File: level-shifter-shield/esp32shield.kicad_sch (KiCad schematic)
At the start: 18 parts, among them J1 Power_Terminal, J2 Screw_Terminal_01x02, J3 Screw_Terminal_01x02, J4 Screw_Terminal_01x02, J5 Screw_Terminal_01x02, J6 Conn_01x19_Female, J7 Conn_01x19_Female, J8 Conn_02x19_Counter_Clockwise, U2 74HC245

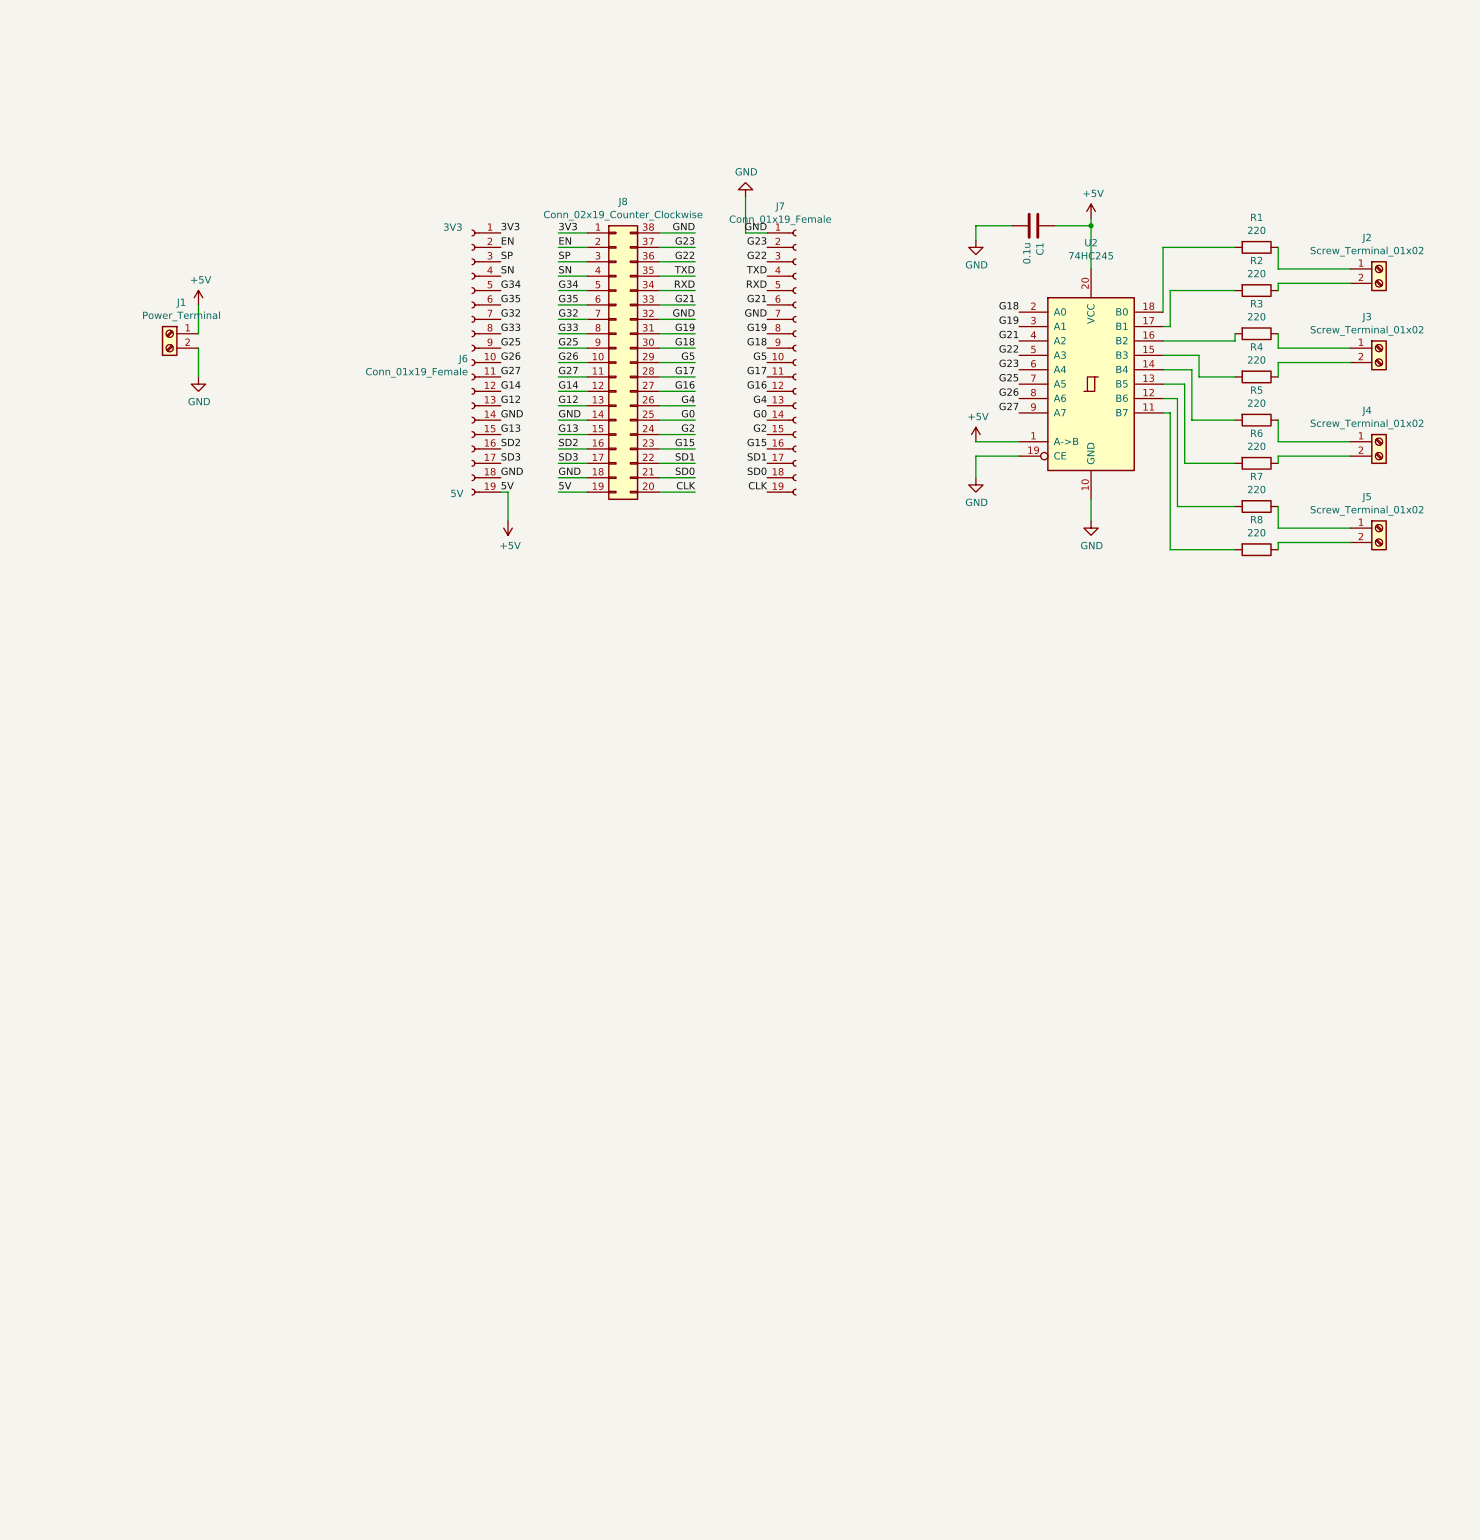
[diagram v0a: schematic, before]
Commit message: Finish new level shifter shield schematic
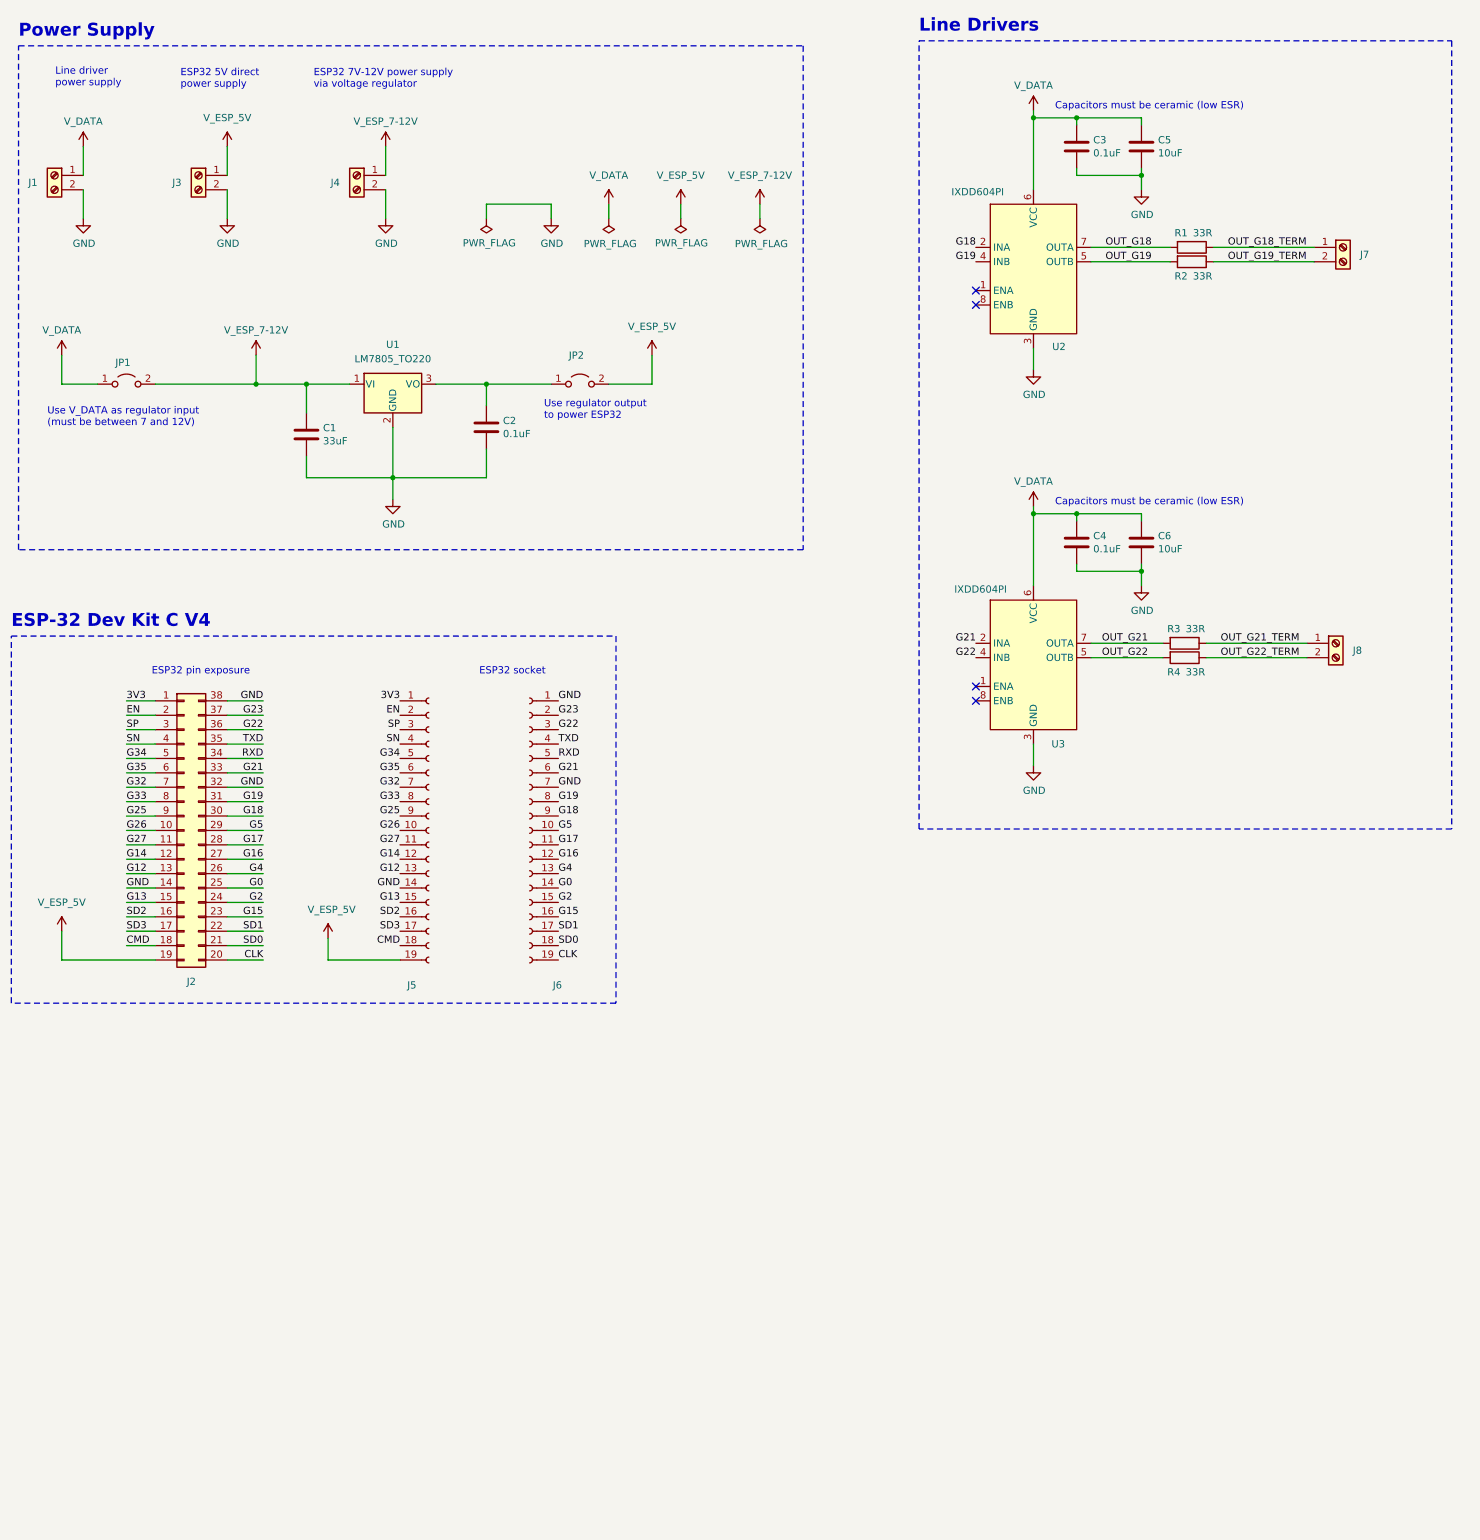
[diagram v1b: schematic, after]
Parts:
- removed J5: Screw_Terminal_01x02, TerminalBlock_Phoenix:TerminalBlock_Phoenix_MKDS-1,5-2-5.08_1x02_P5.08mm_Horizontal, symbol Connector:Screw_Terminal_01x02
- removed J6, J7: Conn_01x19_Female, Connector_PinSocket_2.54mm:PinSocket_1x19_P2.54mm_Vertical, symbol esp32shield-rescue:Conn_01x19_Female-Connector
- removed R5, R6, R7, R8: 220, Resistor_THT:R_Axial_DIN0207_L6.3mm_D2.5mm_P2.54mm_Vertical, symbol Device:R
- removed U2: 74HC245, Package_DIP:DIP-20_W7.62mm, symbol 74xx:74HC245
- added C2, C3, C4: 0.1uF, Capacitor_THT:C_Disc_D3.0mm_W1.6mm_P2.50mm, symbol Device:C
- added C5, C6: 10uF, Capacitor_THT:C_Disc_D3.0mm_W1.6mm_P2.50mm, symbol Device:C
- added J1: Power_Terminal, TerminalBlock_Phoenix:TerminalBlock_Phoenix_MKDS-1,5-2_1x02_P5.00mm_Horizontal, symbol Connector:Screw_Terminal_01x02
- added J5, J6: Conn_01x19_Socket, symbol Connector:Conn_01x19_Socket
- added JP1, JP2: Jumper_2_Open, symbol Jumper:Jumper_2_Open
- added U1: LM7805_TO220, Package_TO_SOT_THT:TO-220-3_Vertical, symbol Regulator_Linear:LM7805_TO220
- added U2, U3: IXDD604PI, Package_DIP:DIP-8_W7.62mm_Socket, symbol lib:IXDD604PI
- C1: value 0.1u -> 33uF
- J4: value Screw_Terminal_01x02 -> Power_Terminal; footprint TerminalBlock_Phoenix:TerminalBlock_Phoenix_MKDS-1,5-2-5.08_1x02_P5.08mm_Horizontal -> TerminalBlock_Phoenix:TerminalBlock_Phoenix_MKDS-1,5-2_1x02_P5.00mm_Horizontal
- R1, R2, R3, R4: value 220 -> 33R
- renumbered J8 to J2, J1 to J3, J2 to J7, J3 to J8
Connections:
- net 3V3: now also J5.1 (Pin_1)
- net CLK: now also J6.19 (Pin_19)
- net EN: now also J5.2 (Pin_2)
- net G0: now also J6.14 (Pin_14)
- net G12: now also J5.13 (Pin_13)
- net G13: now also J5.15 (Pin_15)
- net G14: now also J5.12 (Pin_12)
- net G15: now also J6.16 (Pin_16)
- net G16: now also J6.12 (Pin_12)
- net G17: now also J6.11 (Pin_11)
- net G18: now also J6.9 (Pin_9), U2.2 (INA)
- net G19: now also J6.8 (Pin_8), U2.4 (INB)
- net G2: now also J6.15 (Pin_15)
- net G21: now also J6.6 (Pin_6), U3.2 (INA)
- net G22: now also J6.3 (Pin_3), U3.4 (INB)
- net G23: now also J6.2 (Pin_2)
- net G25: now also J5.9 (Pin_9)
- net G26: now also J5.10 (Pin_10)
- net G27: now also J5.11 (Pin_11)
- net G32: now also J5.7 (Pin_7)
- net G33: now also J5.8 (Pin_8)
- net G34: now also J5.5 (Pin_5)
- net G35: now also J5.6 (Pin_6)
- net G4: now also J6.13 (Pin_13)
- net G5: now also J6.10 (Pin_10)
- net GND: now also J4.2 (Pin_2), C2.2, C3.2, C4.2, C5.2, C6.2, J1.2 (Pin_2), J5.14 (Pin_14), J6.1 (Pin_1), J6.7 (Pin_7), U1.2 (GND), U2.3 (GND), U3.3 (GND); no longer J2.18 (Pin_18)
- net RXD: now also J6.5 (Pin_5)
- net SD0: now also J6.18 (Pin_18)
- net SD1: now also J6.17 (Pin_17)
- net SD2: now also J5.16 (Pin_16)
- net SD3: now also J5.17 (Pin_17)
- net SN: now also J5.4 (Pin_4)
- net SP: now also J5.3 (Pin_3)
- net TXD: now also J6.4 (Pin_4)
- net OUT_G22: now reaches R4.2
- net OUT_G22: now also U3.5 (OUTB)
- net OUT_G21: now reaches R3.2
- net OUT_G21: now also U3.7 (OUTA)
- net OUT_G19: now reaches R2.2
- net OUT_G19: now also U2.5 (OUTB)
- net OUT_G18: now reaches R1.2
- net OUT_G18: now also U2.7 (OUTA)
- net OUT_G18_TERM: now reaches J7.1 (Pin_1), R1.1
- net OUT_G19_TERM: now reaches J7.2 (Pin_2), R2.1
- net OUT_G21_TERM: now reaches J8.1 (Pin_1), R3.1
- net OUT_G22_TERM: now reaches J8.2 (Pin_2), R4.1
- net V_ESP_7-12V: now reaches J4.1 (Pin_1)
- net V_ESP_7-12V: now also C1.1, JP1.2 (B), U1.1 (VI)
- net +5V renamed V_ESP_5V
- net V_ESP_5V: now also J5.19 (Pin_19), JP2.2 (B); no longer C1.1
- new net: C2.1, JP2.1 (A), U1.3 (VO)
- new net CMD: J2.18 (Pin_18), J5.18 (Pin_18)
- new net V_DATA: C3.1, C4.1, C5.1, C6.1, J1.1 (Pin_1), JP1.1 (A), U2.6 (VCC), U3.6 (VCC)
- no-connect marks 0 -> 4
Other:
- note added: "Capacitors must be ceramic (low ESR)"
- note added: "ESP-32 Dev Kit C V4"
- note added: "ESP32 5V direct power supply"
- note added: "ESP32 7V-12V power supply via voltage regulator"
- note added: "ESP32 pin exposure"
- note added: "ESP32 socket"
- note added: "Line Drivers"
- note added: "Line driver power supply"
- note added: "Power Supply"
- note added: "Use V_DATA as regulator input (must be between 7 and 12V)"
- note added: "Use regulator output to power ESP32"
- note removed: "3V3"
- note removed: "5V"
- moved on the sheet: J2, J3, J7, J8

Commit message: Finish level shifter shield layout without traces
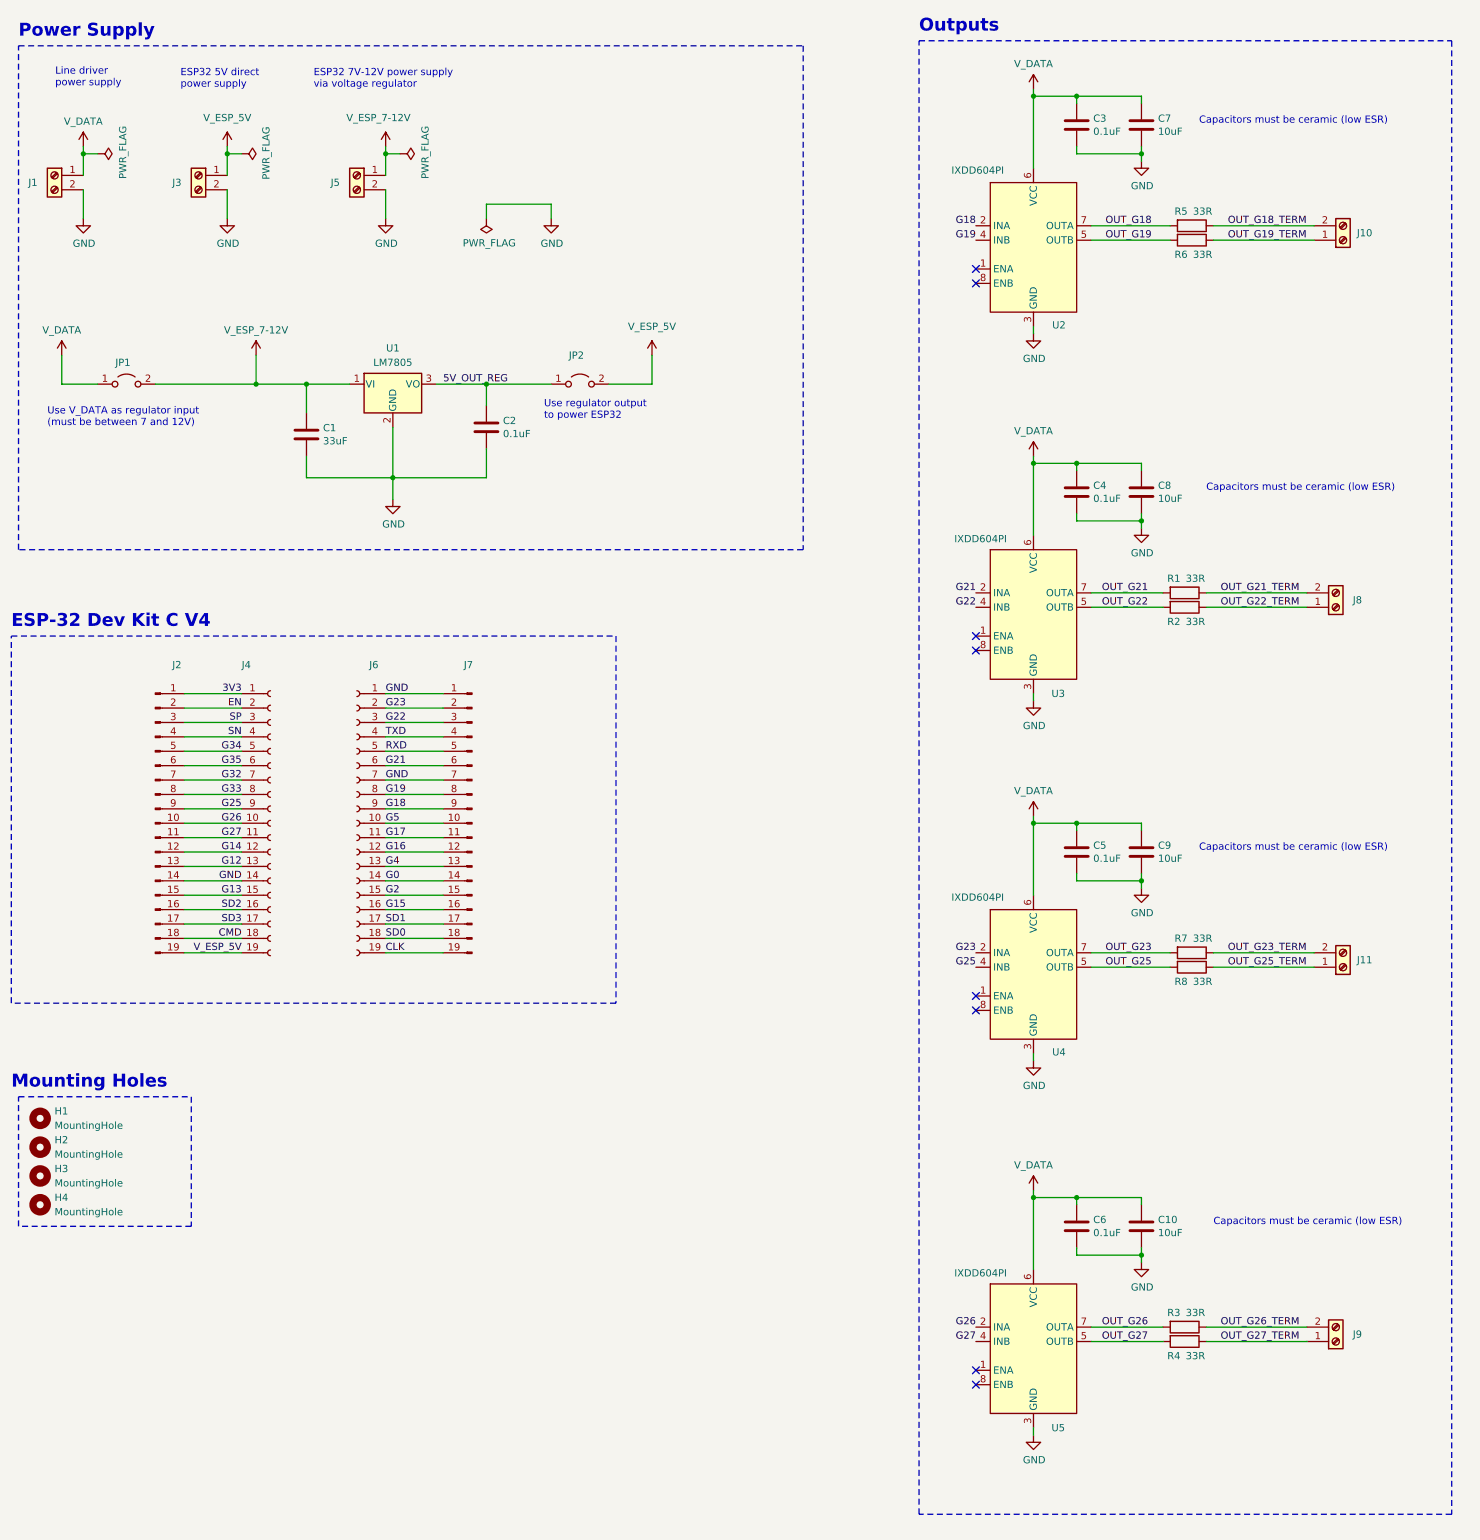
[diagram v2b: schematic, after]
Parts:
- removed J2: Conn_02x19_Counter_Clockwise, Connector_PinHeader_2.54mm:PinHeader_2x19_P2.54mm_Vertical, symbol Connector_Generic:Conn_02x19_Counter_Clockwise
- added C10, C9: 10uF, Capacitor_THT:C_Disc_D3.0mm_W1.6mm_P2.50mm, symbol Device:C
- added C5, C6: 0.1uF, Capacitor_THT:C_Disc_D3.0mm_W1.6mm_P2.50mm, symbol Device:C
- added H1, H2, H3, H4: MountingHole, MountingHole:MountingHole_2.2mm_M2, symbol Mechanical:MountingHole
- added J11, J9: Screw_Terminal_01x02, TerminalBlock_Phoenix:TerminalBlock_Phoenix_MKDS-1,5-2-5.08_1x02_P5.08mm_Horizontal, symbol Connector:Screw_Terminal_01x02
- added J2, J7: Conn_01x19_Pin, Connector_PinHeader_2.54mm:PinHeader_1x19_P2.54mm_Vertical, symbol Connector:Conn_01x19_Pin
- added R3, R4, R7, R8: 33R, Resistor_THT:R_Axial_DIN0207_L6.3mm_D2.5mm_P2.54mm_Vertical, symbol Device:R
- added U4, U5: IXDD604PI, Package_DIP:DIP-8_W7.62mm_Socket, symbol lib:IXDD604PI
- J1, J3: footprint TerminalBlock_Phoenix:TerminalBlock_Phoenix_MKDS-1,5-2_1x02_P5.00mm_Horizontal -> TerminalBlock_Phoenix:TerminalBlock_Phoenix_MKDS-1,5-2-5.08_1x02_P5.08mm_Horizontal
- J4: renamed from J5; footprint (none) -> Connector_PinSocket_2.54mm:PinSocket_1x19_P2.54mm_Vertical
- J5: renamed from J4; footprint TerminalBlock_Phoenix:TerminalBlock_Phoenix_MKDS-1,5-2_1x02_P5.00mm_Horizontal -> TerminalBlock_Phoenix:TerminalBlock_Phoenix_MKDS-1,5-2-5.08_1x02_P5.08mm_Horizontal
- J6: footprint (none) -> Connector_PinSocket_2.54mm:PinSocket_1x19_P2.54mm_Vertical
- JP1, JP2: footprint (none) -> Connector_PinHeader_2.54mm:PinHeader_1x02_P2.54mm_Vertical
- U1: value LM7805_TO220 -> LM7805
- renumbered C5 to C7, C6 to C8, J7 to J10, R3 to R1, R4 to R2, R1 to R5, R2 to R6
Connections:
- net 3V3: now also J2.1 (Pin_1)
- net CLK: now also J7.19 (Pin_19)
- net CMD: now also J2.18 (Pin_18)
- net EN: now also J2.2 (Pin_2)
- net G0: now also J7.14 (Pin_14)
- net G12: now also J2.13 (Pin_13)
- net G13: now also J2.15 (Pin_15)
- net G14: now also J2.12 (Pin_12)
- net G15: now also J7.16 (Pin_16)
- net G16: now also J7.12 (Pin_12)
- net G17: now also J7.11 (Pin_11)
- net G18: now also J7.9 (Pin_9)
- net G19: now also J7.8 (Pin_8)
- net G2: now also J7.15 (Pin_15)
- net G21: now also J7.6 (Pin_6)
- net G22: now also J7.3 (Pin_3)
- net G23: now also J7.2 (Pin_2), U4.2 (INA)
- net G25: now also J2.9 (Pin_9), U4.4 (INB)
- net G26: now also J2.10 (Pin_10), U5.2 (INA)
- net G27: now also J2.11 (Pin_11), U5.4 (INB)
- net G32: now also J2.7 (Pin_7)
- net G33: now also J2.8 (Pin_8)
- net G34: now also J2.5 (Pin_5)
- net G35: now also J2.6 (Pin_6)
- net G4: now also J7.13 (Pin_13)
- net G5: now also J7.10 (Pin_10)
- net GND: now also C10.2, C5.2, C6.2, C9.2, J2.14 (Pin_14), J7.1 (Pin_1), J7.7 (Pin_7), U4.3 (GND), U5.3 (GND)
- net OUT_G18_TERM: now also J10.2 (Pin_2); no longer J10.1 (Pin_1)
- net OUT_G19_TERM: now also J10.1 (Pin_1); no longer J10.2 (Pin_2)
- net OUT_G21_TERM: now also J8.2 (Pin_2); no longer J8.1 (Pin_1)
- net OUT_G22_TERM: now also J8.1 (Pin_1); no longer J8.2 (Pin_2)
- net RXD: now also J7.5 (Pin_5)
- net SD0: now also J7.18 (Pin_18)
- net SD1: now also J7.17 (Pin_17)
- net SD2: now also J2.16 (Pin_16)
- net SD3: now also J2.17 (Pin_17)
- net SN: now also J2.4 (Pin_4)
- net SP: now also J2.3 (Pin_3)
- net TXD: now also J7.4 (Pin_4)
- net V_DATA: now also C10.1, C5.1, C6.1, C9.1, U4.6 (VCC), U5.6 (VCC)
- net V_ESP_5V: now also J2.19 (Pin_19)
- net 5V_OUT_REG: now reaches C2.1, JP2.1 (A), U1.3 (VO)
- new net OUT_G23: R7.2, U4.7 (OUTA)
- new net OUT_G23_TERM: J11.2 (Pin_2), R7.1
- new net OUT_G25: R8.2, U4.5 (OUTB)
- new net OUT_G25_TERM: J11.1 (Pin_1), R8.1
- new net OUT_G26: R3.2, U5.7 (OUTA)
- new net OUT_G26_TERM: J9.2 (Pin_2), R3.1
- new net OUT_G27: R4.2, U5.5 (OUTB)
- new net OUT_G27_TERM: J9.1 (Pin_1), R4.1
- no-connect marks 4 -> 8
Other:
- note added: "Mounting Holes"
- note added: "Outputs"
- note removed: "ESP32 pin exposure"
- note removed: "ESP32 socket"
- note removed: "Line Drivers"
- moved on the sheet: C3, C4, C7, C8, J10, J4, J6, J8, R1, R2, R5, R6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
